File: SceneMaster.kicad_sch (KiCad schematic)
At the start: 102 parts, among them J1 TYPE-C-31-M-12, J11 PowerIn, J12 PowerOut, J13 LED3, J14 LED4, J15 LED5, J2 SPK_R, J3 LED1, J4 LED2, J5 LED6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

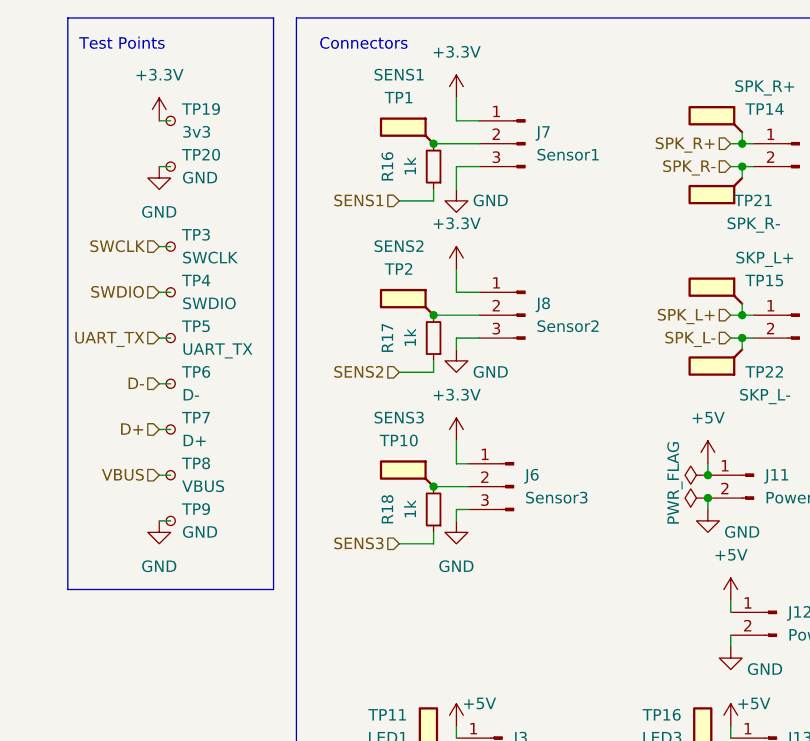
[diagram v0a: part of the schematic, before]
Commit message: Change sensor & speaker connectors to 1mm SH
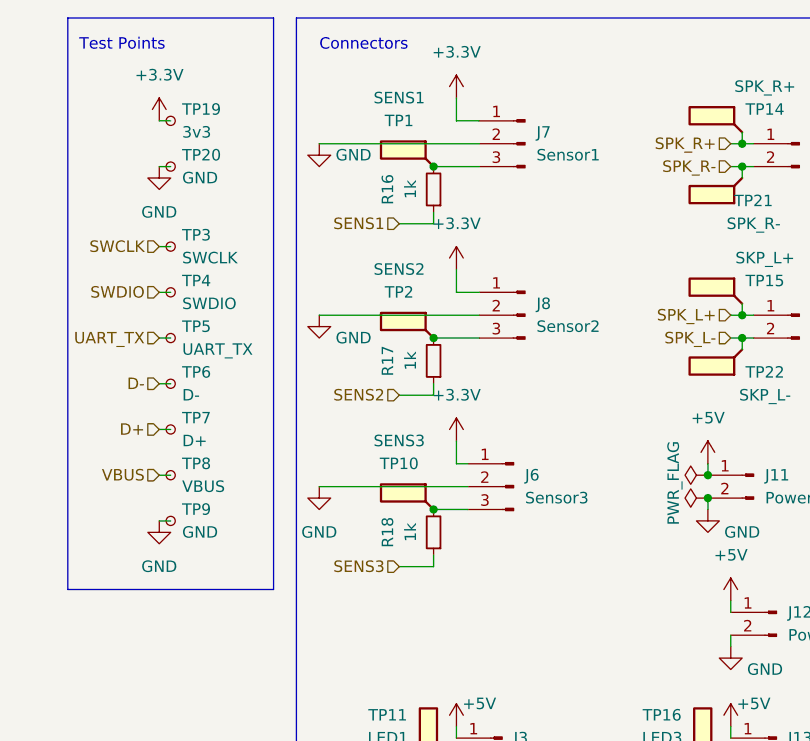
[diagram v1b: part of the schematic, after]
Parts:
- J11, J12, J13, J14, J15, J3, J4, J5: footprint Connector_JST:JST_SUR_SM02B-SURS-TF_1x02-1MP_P0.80mm_Horizontal -> ant:JST_SUR_SM02B-SURS-TF_1x02-1MP_P0.80mm_Horizontal
- J2, J9: footprint Connector_JST:JST_SUR_SM02B-SURS-TF_1x02-1MP_P0.80mm_Horizontal -> ant:JST_SH_SM02B-SRSS-TB_1x02-1MP_P1.00mm_Horizontal
- J6, J7, J8: footprint Connector_JST:JST_SUR_SM03B-SURS-TF_1x03-1MP_P0.80mm_Horizontal -> ant:JST_SH_SM03B-SRSS-TB_1x03-1MP_P1.00mm_Horizontal
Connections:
- net GND: now also J6.2 (Pin_2), J7.2 (Pin_2), J8.2 (Pin_2); no longer J6.3 (Pin_3), J7.3 (Pin_3), J8.3 (Pin_3)
- net at R16.2, TP1.1: now also J7.3 (Pin_3); no longer J7.2 (Pin_2)
- net at R18.2, TP10.1: now also J6.3 (Pin_3); no longer J6.2 (Pin_2)
- net at R17.2, TP2.1: now also J8.3 (Pin_3); no longer J8.2 (Pin_2)
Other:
- moved on the sheet: R16, R17, R18, TP1, TP10, TP2

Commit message: First SGGS re-route
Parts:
- TP14: value SPK_R+ -> SPK_R-
- TP15: value SKP_L+ -> SKP_L-
- TP21: value SPK_R- -> SPK_R+
- TP22: value SKP_L- -> SKP_L+
- TP6, TP7: footprint TestPoint:TestPoint_THTPad_1.0x1.0mm_Drill0.5mm -> TestPoint:TestPoint_Pad_1.0x1.0mm
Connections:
- net D+: no longer TP7.1
- net D-: no longer TP6.1
- net SPK_L+: now also J9.2 (Pin_2), TP22.1; no longer J9.1 (Pin_1), TP15.1
- net SPK_L-: now also J9.1 (Pin_1), TP15.1; no longer J9.2 (Pin_2), TP22.1
- net SPK_R+: now also J2.2 (Pin_2), TP21.1; no longer J2.1 (Pin_1), TP14.1
- net SPK_R-: now also J2.1 (Pin_1), TP14.1; no longer J2.2 (Pin_2), TP21.1
- net USB_DN: now also TP6.1
- net USB_DP: now also TP7.1
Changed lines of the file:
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@@
     (effects (font (size 1.27 1.27)) (justify left))
   )
-  (hierarchical_label "SPK_R+" (shape input) (at 262.89 29.21 180)
+  (hierarchical_label "SPK_R+" (shape input) (at 262.89 31.75 180)
     (effects (font (size 1.27 1.27)) (justify right))
   )
@@
     (effects (font (size 1.27 1.27)) (justify left))
   )
-  (hierarchical_label "SPK_R-" (shape input) (at 262.89 31.75 180)
+  (hierarchical_label "SPK_R-" (shape input) (at 262.89 29.21 180)
     (effects (font (size 1.27 1.27)) (justify right))
   )
@@
     (effects (font (size 1.27 1.27)) (justify left))
   )
+  (hierarchical_label "USB_DN" (shape input) (at 199.39 55.88 180)
+    (effects (font (size 1.27 1.27)) (justify right))
+  )
   (hierarchical_label "Line_Out_L" (shape input) (at 320.04 128.27 180)
     (effects (font (size 1.27 1.27)) (justify right))
@@
     (effects (font (size 1.27 1.27)) (justify left))
   )
-  (hierarchical_label "D-" (shape input) (at 199.39 55.88 180)
+  (hierarchical_label "USB_DP" (shape input) (at 199.39 60.96 180)
     (effects (font (size 1.27 1.27)) (justify right))
   )
@@
     (effects (font (size 1.27 1.27)) (justify left))
   )
-  (hierarchical_label "SPK_L-" (shape input) (at 262.89 50.8 180)
+  (hierarchical_label "SPK_L-" (shape input) (at 262.89 48.26 180)
     (effects (font (size 1.27 1.27)) (justify right))
   )
@@
     (effects (font (size 1.27 1.27)) (justify right))
   )
-  (hierarchical_label "D+" (shape input) (at 199.39 60.96 180)
-    (effects (font (size 1.27 1.27)) (justify right))
-  )
   (hierarchical_label "D+" (shape input) (at 52.07 173.99 0)
     (effects (font (size 1.27 1.27)) (justify left))
@@
     (effects (font (size 1.27 1.27)) (justify right))
   )
-  (hierarchical_label "SPK_L+" (shape input) (at 262.89 48.26 180)
+  (hierarchical_label "SPK_L+" (shape input) (at 262.89 50.8 180)
     (effects (font (size 1.27 1.27)) (justify right))
   )
@@
     (in_bom yes) (on_board yes)
     (property "Reference" "TP15" (id 0) (at 266.7 44.45 0))
-    (property "Value" "SKP_L+" (id 1) (at 266.7 41.91 0))
+    (property "Value" "SKP_L-" (id 1) (at 266.7 41.91 0))
     (property "Footprint" "TestPoint:TestPoint_Pad_1.0x1.0mm" (id 2) (at 259.08 46.99 0)
       (effects (font (size 1.27 1.27)) hide)
@@
     (in_bom yes) (on_board yes)
     (property "Reference" "TP14" (id 0) (at 266.7 25.4 0))
-    (property "Value" "SPK_R+" (id 1) (at 266.7 22.86 0))
+    (property "Value" "SPK_R-" (id 1) (at 266.7 22.86 0))
     (property "Footprint" "TestPoint:TestPoint_Pad_1.0x1.0mm" (id 2) (at 259.08 27.94 0)
       (effects (font (size 1.27 1.27)) hide)
@@
       (effects (font (size 1.27 1.27)) (justify left))
     )
-    (property "Footprint" "TestPoint:TestPoint_THTPad_1.0x1.0mm_Drill0.5mm" (id 2) (at 205.74 55.88 0)
+    (property "Footprint" "TestPoint:TestPoint_Pad_1.0x1.0mm" (id 2) (at 205.74 55.88 0)
       (effects (font (size 1.27 1.27)) hide)
     )
@@
     (in_bom yes) (on_board yes)
     (property "Reference" "TP22" (id 0) (at 266.7 54.61 0))
-    (property "Value" "SKP_L-" (id 1) (at 266.7 57.15 0))
+    (property "Value" "SKP_L+" (id 1) (at 266.7 57.15 0))
     (property "Footprint" "TestPoint:TestPoint_Pad_1.0x1.0mm" (id 2) (at 259.08 52.07 0)
       (effects (font (size 1.27 1.27)) hide)
@@
       (effects (font (size 1.27 1.27)) (justify left))
     )
-    (property "Footprint" "TestPoint:TestPoint_THTPad_1.0x1.0mm_Drill0.5mm" (id 2) (at 205.74 60.96 0)
+    (property "Footprint" "TestPoint:TestPoint_Pad_1.0x1.0mm" (id 2) (at 205.74 60.96 0)
       (effects (font (size 1.27 1.27)) hide)
     )
@@
     (in_bom yes) (on_board yes)
     (property "Reference" "TP21" (id 0) (at 265.43 35.56 0))
-    (property "Value" "SPK_R-" (id 1) (at 265.43 38.1 0))
+    (property "Value" "SPK_R+" (id 1) (at 265.43 38.1 0))
     (property "Footprint" "TestPoint:TestPoint_Pad_1.0x1.0mm" (id 2) (at 259.08 33.02 0)
       (effects (font (size 1.27 1.27)) hide)
@@
     )
     (path "/661af687-9032-4599-9383-d8fac0fabe9e"
-      (reference "TP6") (unit 1) (value "D-") (footprint "TestPoint:TestPoint_THTPad_1.0x1.0mm_Drill0.5mm")
+      (reference "TP6") (unit 1) (value "D-") (footprint "TestPoint:TestPoint_Pad_1.0x1.0mm")
     )
     (path "/dc50e65e-80e3-4ac1-b9b1-a96719d002f6"
-      (reference "TP7") (unit 1) (value "D+") (footprint "TestPoint:TestPoint_THTPad_1.0x1.0mm_Drill0.5mm")
+      (reference "TP7") (unit 1) (value "D+") (footprint "TestPoint:TestPoint_Pad_1.0x1.0mm")
     )
     (path "/1f3c309e-5ae6-48cb-ab60-3aad9d93db60"
@@
     )
     (path "/654dd74d-e95b-4009-91af-aec62593dd66"
-      (reference "TP14") (unit 1) (value "SPK_R+") (footprint "TestPoint:TestPoint_Pad_1.0x1.0mm")
+      (reference "TP14") (unit 1) (value "SPK_R-") (footprint "TestPoint:TestPoint_Pad_1.0x1.0mm")
     )
     (path "/4d05b96a-6fbe-4e1e-9927-c6a14fd564d1"
-      (reference "TP15") (unit 1) (value "SKP_L+") (footprint "TestPoint:TestPoint_Pad_1.0x1.0mm")
+      (reference "TP15") (unit 1) (value "SKP_L-") (footprint "TestPoint:TestPoint_Pad_1.0x1.0mm")
     )
     (path "/a80ca190-727d-471b-8e5a-07faa6abe6c6"
@@
     )
     (path "/ffe8251c-66f9-410a-9e31-1d6eb1cf0915"
-      (reference "TP21") (unit 1) (value "SPK_R-") (footprint "TestPoint:TestPoint_Pad_1.0x1.0mm")
+      (reference "TP21") (unit 1) (value "SPK_R+") (footprint "TestPoint:TestPoint_Pad_1.0x1.0mm")
     )
     (path "/66a0b26b-c5a4-425f-aa45-d46e54ed1cfd"
-      (reference "TP22") (unit 1) (value "SKP_L-") (footprint "TestPoint:TestPoint_Pad_1.0x1.0mm")
+      (reference "TP22") (unit 1) (value "SKP_L+") (footprint "TestPoint:TestPoint_Pad_1.0x1.0mm")
     )
     (path "/cdd71c94-85e1-4010-86ab-dba36a6b66c6"

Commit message: Last changes before prototype run
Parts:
- removed TP19: 3v3, TestPoint:TestPoint_THTPad_1.0x1.0mm_Drill0.5mm, symbol Connector:TestPoint_Small
- removed TP20: GND, TestPoint:TestPoint_THTPad_1.0x1.0mm_Drill0.5mm, symbol Connector:TestPoint_Small
- removed TP3: SWCLK, TestPoint:TestPoint_THTPad_1.0x1.0mm_Drill0.5mm, symbol Connector:TestPoint_Small
- removed TP4: SWDIO, TestPoint:TestPoint_THTPad_1.0x1.0mm_Drill0.5mm, symbol Connector:TestPoint_Small
- removed TP5: UART_TX, TestPoint:TestPoint_Pad_1.0x1.0mm, symbol Connector:TestPoint_Small
- added J10: Conn_01x08_Male, ant:SOIC_clipProgSmall, symbol Connector:Conn_01x08_Male
- FB1, FB2: value 600Ω@100MHz -> 100Ω@100MHz; MPN C1017 -> C1015
- J2, J9: footprint ant:JST_SH_SM02B-SRSS-TB_1x02-1MP_P1.00mm_Horizontal -> Connector_Hirose:Hirose_DF13C_CL535-0402-2-51_1x02-1MP_P1.25mm_Vertical; MPN C2845343 -> C2905009
- J6, J7, J8: MPN C2845344 -> C2936213
- R20, R21, R24, R25: MPN (none) -> C25765
- U5, U6: JlcRotOffset (none) -> -90; MPN (none) -> C329450
- Y1: footprint Crystal:Crystal_SMD_5032-2Pin_5.0x3.2mm -> Crystal:Crystal_SMD_TXC_7A-2Pin_5x3.2mm
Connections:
- net +5V: now also J10.4 (Pin_4)
- net GND: now also J10.3 (Pin_3), J10.5 (Pin_5), J10.6 (Pin_6), J10.7 (Pin_7)
- net MUTE: now also U4.19 (PB1)
- net SWCLK: now also J10.1 (Pin_1)
- net SWDIO: now also J10.2 (Pin_2)
- net UART_TX: now also J10.8 (Pin_8)
- no-connect marks 22 -> 21

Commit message: Add gate resistor to mosfets
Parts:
- added R26, R27, R28, R29, R30, R31: 1k, Resistor_SMD:R_0402_1005Metric, symbol Device:R_Small
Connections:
- net LED1: now also R26.2; no longer Q1.1 (G)
- net LED2: now also R27.2; no longer Q2.1 (G)
- net LED3: now also R29.2; no longer Q4.1 (G)
- net LED4: now also R30.2; no longer Q5.1 (G)
- net LED5: now also R31.2; no longer Q6.1 (G)
- net LED6: now also R28.2; no longer Q3.1 (G)
- new net: Q1.1 (G), R26.1
- new net: Q5.1 (G), R30.1
- new net: Q6.1 (G), R31.1
- new net: Q2.1 (G), R27.1
- new net: Q4.1 (G), R29.1
- new net: Q3.1 (G), R28.1
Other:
- moved on the sheet: J13, J14, J15, J3, J4, J5, Q1, Q2, Q3, Q4, Q5, Q6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

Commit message: Add USB enable pull up
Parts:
- added R32: 1k5, Resistor_SMD:R_0402_1005Metric, symbol Device:R_Small
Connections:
- net USB_DP: now also R32.1
- net USB_EN: now also R32.2
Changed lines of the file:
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@@
   (junction (at 57.15 74.93) (diameter 0) (color 0 0 0 0)
   )
+  (junction (at 50.8 168.91) (diameter 0) (color 0 0 0 0)
+  )
   (junction (at 148.59 142.24) (diameter 0) (color 0 0 0 0)
   )
@@
     (stroke (width 0) (type default) (color 0 0 0 0))
   )
-  (wire (pts (xy 49.53 168.91) (xy 52.07 168.91))
+  (wire (pts (xy 49.53 168.91) (xy 50.8 168.91))
     (stroke (width 0) (type default) (color 0 0 0 0))
   )
@@
     (stroke (width 0) (type default) (color 0 0 0 0))
   )
+  (wire (pts (xy 50.8 166.37) (xy 50.8 168.91))
+    (stroke (width 0) (type default) (color 0 0 0 0))
+  )
   (wire (pts (xy 69.85 36.83) (xy 69.85 41.91))
     (stroke (width 0) (type default) (color 0 0 0 0))
@@
     (stroke (width 0) (type default) (color 0 0 0 0))
   )
+  (wire (pts (xy 50.8 168.91) (xy 52.07 168.91))
+    (stroke (width 0) (type default) (color 0 0 0 0))
+  )
   (wire (pts (xy 83.82 26.67) (xy 92.71 26.67))
     (stroke (width 0) (type default) (color 0 0 0 0))
@@
     (effects (font (size 1.27 1.27)) (justify right))
   )
+  (hierarchical_label "USB_EN" (shape input) (at 50.8 161.29 90)
+    (effects (font (size 1.27 1.27)) (justify left))
+  )
   (hierarchical_label "D+" (shape input) (at 52.07 173.99 0)
     (effects (font (size 1.27 1.27)) (justify left))
@@
     (pin "1")
   )
+  (symbol (lib_id "Device:R_Small") (at 50.8 163.83 180) (unit 1)
+    (in_bom yes) (on_board yes)
+    (property "Reference" "R32" (id 0) (at 52.07 163.83 0)
+      (effects (font (size 1.27 1.27)) (justify right))
+    )
+    (property "Value" "1k5" (id 1) (at 52.07 166.37 0)
+      (effects (font (size 1.27 1.27)) (justify right))
+    )
+    (property "Footprint" "Resistor_SMD:R_0402_1005Metric" (id 2) (at 50.8 163.83 0)
+      (effects (font (size 1.27 1.27)) hide)
+    )
+    (property "Datasheet" "~" (id 3) (at 50.8 163.83 0)
+      (effects (font (size 1.27 1.27)) hide)
+    )
+    (property "MPN" "C25867" (id 4) (at 50.8 163.83 0)
+      (effects (font (size 1.27 1.27)) hide)
+    )
+    (pin "1")
+    (pin "2")
+  )
   (symbol (lib_id "Device:R_Small") (at 82.55 63.5 180) (unit 1)
     (in_bom yes) (on_board yes)
@@
   )
   (symbol (lib_id "Power_Protection:USBLC6-2P6") (at 39.37 171.45 0) (unit 1)
-    (in_bom yes) (on_board yes) (fields_autoplaced)
-    (property "Reference" "U1" (id 0) (at 42.1387 158.75 0)
+    (in_bom yes) (on_board yes)
+    (property "Reference" "U1" (id 0) (at 24.13 158.75 0)
       (effects (font (size 1.27 1.27)) (justify left))
     )
-    (property "Value" "USBLC6-2P6" (id 1) (at 42.1387 161.29 0)
+    (property "Value" "USBLC6-2P6" (id 1) (at 24.13 161.29 0)
       (effects (font (size 1.27 1.27)) (justify left))
     )
@@
       (reference "R31") (unit 1) (value "1k") (footprint "Resistor_SMD:R_0402_1005Metric")
     )
+    (path "/c50863fc-3513-489f-9cf4-615e9222e0e2"
+      (reference "R32") (unit 1) (value "1k5") (footprint "Resistor_SMD:R_0402_1005Metric")
+    )
     (path "/a36a0ea6-0703-4e0e-8d2f-039b3ce46a99"

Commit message: Change programming port
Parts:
- added TP19: 5V, TestPoint:TestPoint_THTPad_1.0x1.0mm_Drill0.5mm, symbol Connector:TestPoint_Small
- added TP20: GND, TestPoint:TestPoint_THTPad_1.0x1.0mm_Drill0.5mm, symbol Connector:TestPoint_Small
- added TP23: NRST, TestPoint:TestPoint_THTPad_1.0x1.0mm_Drill0.5mm, symbol Connector:TestPoint_Small
- added TP3: SWDIO, TestPoint:TestPoint_THTPad_1.0x1.0mm_Drill0.5mm, symbol Connector:TestPoint_Small
- added TP4: SWCLK, TestPoint:TestPoint_THTPad_1.0x1.0mm_Drill0.5mm, symbol Connector:TestPoint_Small
- added TP5: UARTTX, TestPoint:TestPoint_THTPad_1.0x1.0mm_Drill0.5mm, symbol Connector:TestPoint_Small
- C10, C8: value 2.2u -> 470n; MPN C12530 -> C47339
- R12, R13, R15, R16, R17, R18, R22, R26, R27, R28, R29, R3, R30, R31, R4, R5, R6, R7: value 1k -> 1k5; MPN C11702 -> C25867
- R21, R25: value 20k -> 33k; MPN C25765 -> C25779
- R8, R9: MPN C25905 -> C25133
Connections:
- net +5V: now also TP19.1
- net GND: now also TP20.1
- net Line_Out_L: now also C10.1, C11.1, R9.2; no longer C10.2, R24.2
- net Line_Out_R: now also C8.1, C9.1, R8.2; no longer C8.2, R20.2
- net SWCLK: now also TP4.1
- net SWDIO: now also TP3.1
- net UART_TX: now also TP5.1
- net NRST: now reaches C15.2, U4.7 (NRST)
- net NRST: now also TP23.1
- new net: C10.2, R24.2
- new net: C8.2, R20.2
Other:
- moved on the sheet: C10, C15, C8

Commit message: add license
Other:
- note added: "SPDX-FileCopyrightText: 2023 Antonios Vamporakis <ant@anttronics.com> SPDX-License-Identifier: CERN-OHL-W-2.0+ You may redistribute and modify this documentation and make products using it under the terms of the CERN-OHL-W v2 (https:/cern.ch/cern-ohl). This documentation is distributed WITHOUT ANY EXPRESS OR IMPLIED WARRANTY, INCLUDING OF MERCHANTABILITY, SATISFACTORY QUALITY AND FITNESS FOR A PA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"
- company: (none) -> AntTronics
- title: (none) -> SceneMaster
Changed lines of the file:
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@@
 (kicad_sch (version 20211123) (generator eeschema)
   (paper "A4")
+  (title_block
+    (title "SceneMaster")
+    (date "2023-12-21")
+    (rev "0.1")
+    (company "AntTronics")
+  )
   (junction (at 236.22 143.51) (diameter 0) (color 0 0 0 0)
   )
@@
     (stroke (width 0) (type default) (color 0 0 0 0))
   )
+  (text "SPDX-FileCopyrightText: 2023 Antonios Vamporakis <ant@anttronics.com>\nSPDX-License-Identifier: CERN-OHL-W-2.0+\n\nYou may redistribute and modify this documentation and make products\nusing it under the terms of the CERN-OHL-W v2 (https:/cern.ch/cern-ohl).\nThis documentation is distributed WITHOUT ANY EXPRESS OR IMPLIED\nWARRANTY, INCLUDING OF MERCHANTABILITY, SATISFACTORY QUALITY\nAND FITNESS FOR A PARTICULAR PURPOSE. Please see the CERN-OHL-W v2\nfor applicable conditions.\n\nSource location: https://github.com/anttronics/SolarTrackerSensor\n\nAs per CERN-OHL-W v2 section 4.1, should You produce hardware based on\nthese sources, You must maintain the Source Location visible on the\nexternal case of the SceneMaster or other product you make using\nthis documentation.\n"
+    (at 236.22 186.69 0)
+    (effects (font (size 0.8 0.8)) (justify left bottom))
+  )
   (text "Connectors" (at 217.17 19.05 0)
